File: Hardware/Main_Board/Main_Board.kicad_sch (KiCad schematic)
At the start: 0 parts

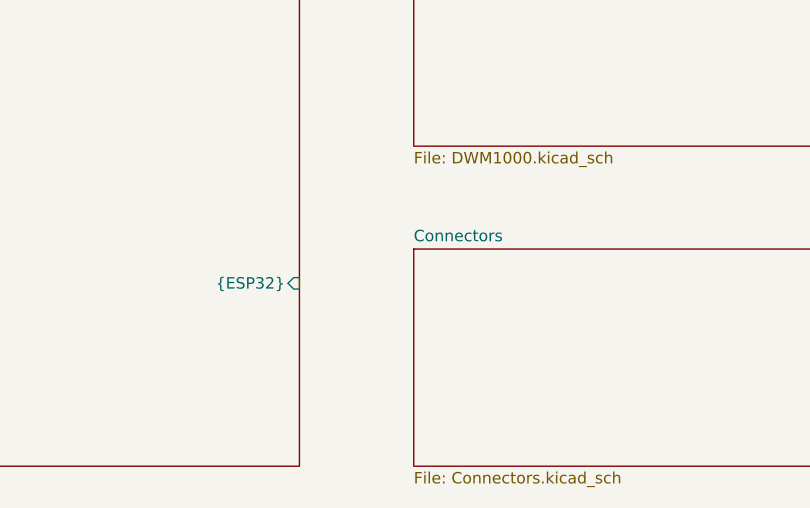
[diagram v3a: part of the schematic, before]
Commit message: Added all the main connectors
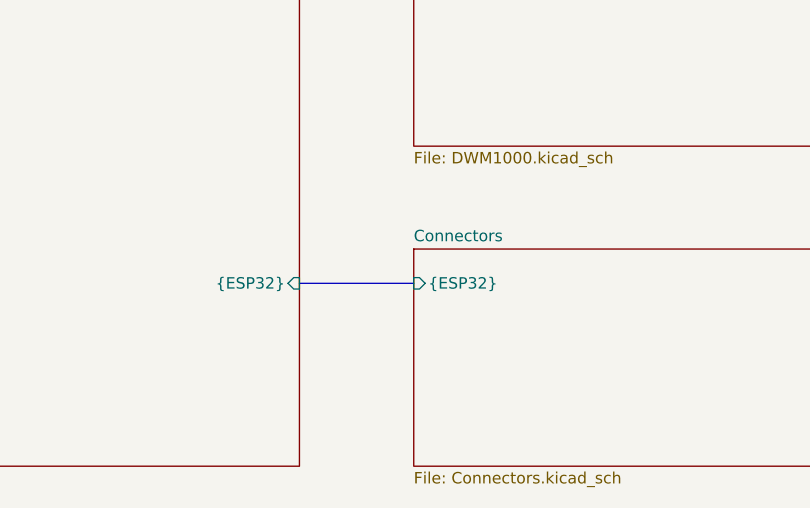
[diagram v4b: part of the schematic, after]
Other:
- sheet Connectors ports: added {ESP32}; removed none
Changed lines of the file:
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@@
+		)
+	)
+	(bus
+		(pts
+			(xy 80.01 142.24) (xy 92.71 142.24)
+		)
+		(stroke
+			(width 0)
+			(type default)
 		)
 	)
@@
 			)
 		)
+		(pin "{ESP32}" input
+			(at 92.71 142.24 180)
+			(effects
+				(font
+					(size 1.27 1.27)
+				)
+				(justify left)
+			)
+		)
